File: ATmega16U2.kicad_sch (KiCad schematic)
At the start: 29 parts, among them J1 Conn_02x02_Odd_Even, J11 Conn_02x03_Odd_Even, J12 USB_B, U3 ATmega16U2-A, Y2 Crystal

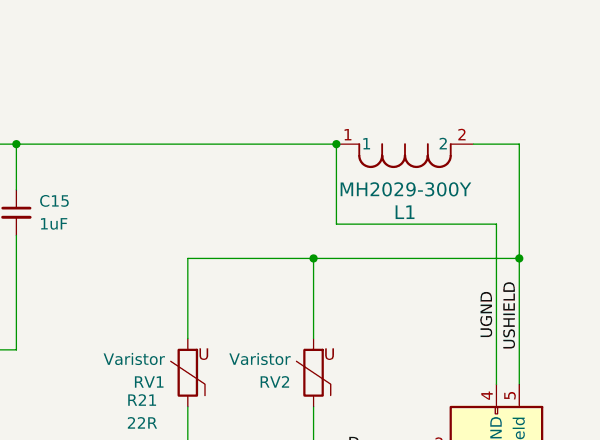
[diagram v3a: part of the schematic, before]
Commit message: finished editing the schematic and assigning footprints
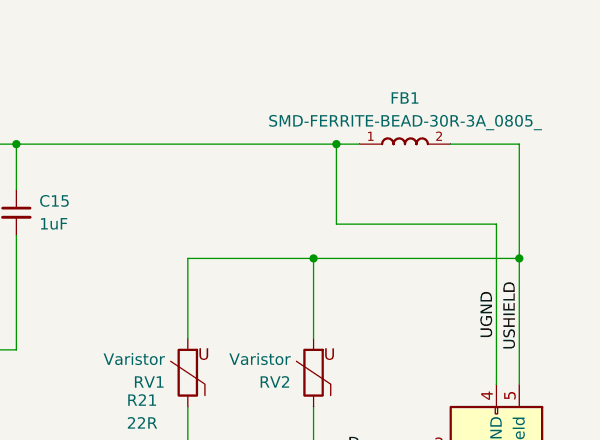
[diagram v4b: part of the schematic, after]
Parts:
- removed L1: MH2029-300Y, IND_BOURNS_MH2029, symbol MH2029_300Y:MH2029-300Y
- added FB1: SMD-FERRITE-BEAD-30R-3A_0805_, SMD-FERRITE-BEAD-30R-3A_0805_:L0805, symbol SMD-FERRITE-BEAD-30R-3A_0805_:SMD-FERRITE-BEAD-30R-3A_0805_
- J1: footprint (none) -> Connector_Hirose:Hirose_DF11-4DP-2DSA_2x02_P2.00mm_Vertical
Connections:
- net 1: now also FB1.1
- net USHIELD: now also FB1.2
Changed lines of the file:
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@@
 	)
 	(junction
+		(at 215.9 45.72)
+		(diameter 0)
+		(color 0 0 0 0)
+	)
+	(junction
 		(at 116.84 167.64)
 		(diameter 0)
@@
 	)
 	(junction
-		(at 215.9 45.72)
-		(diameter 0)
-		(color 0 0 0 0)
-	)
-	(junction
 		(at 58.42 74.93)
 		(diameter 0)
@@
 	(wire
 		(pts
+			(xy 228.6 45.72) (xy 236.22 45.72)
+		)
+		(stroke
+			(width 0)
+			(type default)
+		)
+	)
+	(wire
+		(pts
 			(xy 58.42 64.77) (xy 58.42 74.93)
 		)
@@
 	(wire
 		(pts
+			(xy 215.9 45.72) (xy 218.44 45.72)
+		)
+		(stroke
+			(width 0)
+			(type default)
+		)
+	)
+	(wire
+		(pts
 			(xy 124.46 152.4) (xy 124.46 148.59)
 		)
@@
 	(wire
 		(pts
-			(xy 236.22 45.72) (xy 231.14 45.72)
-		)
-		(stroke
-			(width 0)
-			(type default)
-		)
-	)
-	(wire
-		(pts
 			(xy 233.68 54.61) (xy 215.9 54.61)
 		)
@@
 			)
 		)
-		(property "Footprint" ""
+		(property "Footprint" "Connector_Hirose:Hirose_DF11-4DP-2DSA_2x02_P2.00mm_Vertical"
 			(at 78.74 100.33 0)
 			(effects
@@
 	)
 	(symbol
+		(lib_id "SMD-FERRITE-BEAD-30R-3A_0805_:SMD-FERRITE-BEAD-30R-3A_0805_")
+		(at 223.52 45.72 0)
+		(unit 1)
+		(exclude_from_sim no)
+		(in_bom yes)
+		(on_board yes)
+		(dnp no)
+		(fields_autoplaced yes)
+		(property "Reference" "FB1"
+			(at 223.52 40.64 0)
+			(effects
+				(font
+					(size 1.27 1.27)
+				)
+			)
+		)
+		(property "Value" "SMD-FERRITE-BEAD-30R-3A_0805_"
+			(at 223.52 43.18 0)
+			(effects
+				(font
+					(size 1.27 1.27)
+				)
+			)
+		)
+		(property "Footprint" "SMD-FERRITE-BEAD-30R-3A_0805_:L0805"
+			(at 223.52 45.72 0)
+			(effects
+				(font
+					(size 1.27 1.27)
+				)
+				(justify bottom)
+				(hide yes)
+			)
+		)
+		(property "Datasheet" ""
+			(at 223.52 45.72 0)
+			(effects
+				(font
+					(size 1.27 1.27)
+				)
+				(hide yes)
+			)
+		)
+		(property "Description" ""
+			(at 223.52 45.72 0)
+			(effects
+				(font
+					(size 1.27 1.27)
+				)
+				(hide yes)
+			)
+		)
+		(property "MF" "Bourns"
+			(at 223.52 45.72 0)
+			(effects
+				(font
+					(size 1.27 1.27)
+				)
+				(justify bottom)
+				(hide yes)
+			)
+		)
+		(property "Description_1" "\nCB2x1.2x.9mm, 30?25%3A, non-shdSMD | Bourns MH2029-300Y\n"
+			(at 223.52 45.72 0)
+			(effects
+				(font
+					(size 1.27 1.27)
+				)
+				(justify bottom)
+				(hide yes)
+			)
+		)
+		(property "Package" "0805 Bourns"
+			(at 223.52 45.72 0)
+			(effects
+				(font
+					(size 1.27 1.27)
+				)
+				(justify bottom)
+				(hide yes)
+			)
+		)
+		(property "MPN" "MH2029-300Y"
+			(at 223.52 45.72 0)
+			(effects
+				(font
+					(size 1.27 1.27)
+				)
+				(justify bottom)
+				(hide yes)
+			)
+		)
+		(property "Price" "None"
+			(at 223.52 45.72 0)
+			(effects
+				(font
+					(size 1.27 1.27)
+				)
+				(justify bottom)
+				(hide yes)
+			)
+		)
+		(property "VALUE" "30R 3A"
+			(at 223.52 45.72 0)
+			(effects
+				(font
+					(size 1.27 1.27)
+				)
+				(justify bottom)
+				(hide yes)
+			)
+		)
+		(property "SnapEDA_Link" "https://www.snapeda.com/parts/MH2029-300Y/Bourns+-+J.W.+Miller/view-part/?ref=snap"
+			(at 223.52 45.72 0)
+			(effects
+				(font
+					(size 1.27 1.27)
+				)
+				(justify bottom)
+				(hide yes)
+			)
+		)
+		(property "MP" "MH2029-300Y"
+			(at 223.52 45.72 0)
+			(effects
+				(font
+					(size 1.27 1.27)
+				)
+				(justify bottom)
+				(hide yes)
+			)
+		)
+		(property "Purchase-URL" "https://www.snapeda.com/api/url_track_click_mouser/?unipart_id=42623&manufacturer=Bourns&part_name=MH2029-300Y&search_term=mh2029"
+			(at 223.52 45.72 0)
+			(effects
+				(font
+					(size 1.27 1.27)
+				)
+				(justify bottom)
+				(hide yes)
+			)
+		)
+		(property "Availability" "In Stock"
+			(at 223.52 45.72 0)
+			(effects
+				(font
+					(size 1.27 1.27)
+				)
+				(justify bottom)
+				(hide yes)
+			)
+		)
+		(property "Check_prices" "https://www.snapeda.com/parts/MH2029-300Y/Bourns+-+J.W.+Miller/view-part/?ref=eda"
+			(at 223.52 45.72 0)
+			(effects
+				(font
+					(size 1.27 1.27)
+				)
+				(justify bottom)
+				(hide yes)
+			)
+		)
+		(pin "2"
+		)
+		(pin "1"
+		)
+		(instances
+			(project ""
+				(path "/01593c05-32ee-43cc-9d3f-a6fed62a39f4/b6f834a9-11ca-4a09-9cf4-5366685f0c51"
+					(reference "FB1")
+					(unit 1)
+				)
+			)
+		)
+	)
+	(symbol
 		(lib_id "Device:C_Small")
 		(at 200.66 92.71 0)
@@
 					(unit 1)
 				)
-			)
-		)
-	)
-	(symbol
-		(lib_id "MH2029_300Y:MH2029-300Y")
-		(at 231.14 45.72 180)
-		(unit 1)
-		(exclude_from_sim no)
-		(in_bom yes)
-		(on_board yes)
-		(dnp no)
-		(fields_autoplaced yes)
-		(property "Reference" "L1"
-			(at 223.52 53.34 0)
-			(effects
-				(font
-					(size 1.524 1.524)
-				)
-			)
-		)
-		(property "Value" "MH2029-300Y"
-			(at 223.52 50.8 0)
-			(effects
-				(font
-					(size 1.524 1.524)
-				)
-			)
-		)
-		(property "Footprint" "IND_BOURNS_MH2029"
-			(at 231.14 45.72 0)
-			(effects
-				(font
-					(size 1.27 1.27)
-					(italic yes)
-				)
-				(hide yes)
-			)
-		)
-		(property "Datasheet" "MH2029-300Y"
-			(at 231.14 45.72 0)
-			(effects
-				(font
-					(size 1.27 1.27)
-					(italic yes)
-				)
-				(hide yes)
-			)
-		)
-		(property "Description" ""
-			(at 231.14 45.72 0)
-			(effects
-				(font
-					(size 1.27 1.27)
-				)
-				(hide yes)
-			)
-		)
-		(pin "1"
-		)
-		(pin "2"
-		)
-		(instances
-			(project "arduino-mega-2560"
-				(path "/01593c05-32ee-43cc-9d3f-a6fed62a39f4/b6f834a9-11ca-4a09-9cf4-5366685f0c51"
-					(reference "L1")
-					(unit 1)
-				)

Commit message: started PCB design
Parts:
- Y2: footprint MCU-ATMEGA2560-16AU_TQFP100:TQFP100-0.5-14X14MM -> Crystal:Crystal_SMD_HC49-SD_HandSoldering
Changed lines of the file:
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@@
 			)
 		)
-		(property "Footprint" "MCU-ATMEGA2560-16AU_TQFP100:TQFP100-0.5-14X14MM"
+		(property "Footprint" "Crystal:Crystal_SMD_HC49-SD_HandSoldering"
 			(at 181.61 109.22 0)
 			(effects

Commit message: last save attempt
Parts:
- J1: footprint Connector_Hirose:Hirose_DF11-4DP-2DSA_2x02_P2.00mm_Vertical -> Connector_PinHeader_1.00mm:PinHeader_2x02_P1.00mm_Vertical
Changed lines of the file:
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@@
 			)
 		)
-		(property "Footprint" "Connector_Hirose:Hirose_DF11-4DP-2DSA_2x02_P2.00mm_Vertical"
+		(property "Footprint" "Connector_PinHeader_1.00mm:PinHeader_2x02_P1.00mm_Vertical"
 			(at 78.74 100.33 0)
 			(effects

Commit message: good progress
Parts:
- removed Y2: Crystal, Crystal:Crystal_SMD_HC49-SD_HandSoldering, symbol Device:Crystal
- added Y3: ECS-160-20-4X-B-DN, ECS_160_20_4X_B_DN:XTAL_ECS-160-20-4X-B-DN, symbol ECS-160-20-4X-B-DN:ECS-160-20-4X-B-DN
- RR1: renamed from 1M1; value R -> 1M
- RV1, RV2: footprint Varistor:Varistor_Panasonic_VF -> Resistor_SMD:R_0201_0603Metric_Pad0.64x0.40mm_HandSolder
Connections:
- net 1: now also Y3.1, Y3.2
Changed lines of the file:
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@@
 	)
 	(junction
-		(at 191.77 113.03)
+		(at 191.77 104.14)
 		(diameter 0)
 		(color 0 0 0 0)
@@
 	)
 	(junction
+		(at 180.34 104.14)
+		(diameter 0)
+		(color 0 0 0 0)
+	)
+	(junction
 		(at 166.37 45.72)
 		(diameter 0)
@@
 	)
 	(junction
-		(at 200.66 87.63)
+		(at 191.77 114.3)
 		(diameter 0)
 		(color 0 0 0 0)
 	)
 	(junction
-		(at 154.94 127)
+		(at 200.66 87.63)
 		(diameter 0)
 		(color 0 0 0 0)
 	)
 	(junction
-		(at 181.61 113.03)
+		(at 154.94 127)
 		(diameter 0)
 		(color 0 0 0 0)
@@
 	)
 	(junction
-		(at 181.61 105.41)
-		(diameter 0)
-		(color 0 0 0 0)
-	)
-	(junction
 		(at 236.22 58.42)
 		(diameter 0)
@@
 	)
 	(junction
-		(at 191.77 105.41)
+		(at 58.42 74.93)
 		(diameter 0)
 		(color 0 0 0 0)
 	)
 	(junction
-		(at 58.42 74.93)
+		(at 180.34 114.3)
 		(diameter 0)
 		(color 0 0 0 0)
@@
 		(at 137.16 86.36)
 	)
+	(bus_entry
+		(at 53.34 78.74)
+		(size 2.54 2.54)
+		(stroke
+			(width 0)
+			(type default)
+		)
+	)
 	(wire
 		(pts
@@
 	(wire
 		(pts
-			(xy 191.77 113.03) (xy 181.61 113.03)
+			(xy 110.49 137.16) (xy 110.49 146.05)
 		)
 		(stroke
@@
 	(wire
 		(pts
-			(xy 110.49 137.16) (xy 110.49 146.05)
+			(xy 154.94 53.34) (xy 154.94 39.37)
 		)
 		(stroke
@@
 	(wire
 		(pts
-			(xy 154.94 53.34) (xy 154.94 39.37)
+			(xy 58.42 74.93) (xy 53.34 74.93)
 		)
 		(stroke
@@
 	(wire
 		(pts
-			(xy 58.42 74.93) (xy 53.34 74.93)
+			(xy 199.39 82.55) (xy 198.12 82.55)
 		)
 		(stroke
@@
 	(wire
 		(pts
-			(xy 199.39 82.55) (xy 198.12 82.55)
+			(xy 172.72 104.14) (xy 172.72 106.68)
 		)
 		(stroke
@@
 	(wire
 		(pts
-			(xy 176.53 113.03) (xy 181.61 113.03)
+			(xy 176.53 114.3) (xy 180.34 114.3)
 		)
 		(stroke
@@
 	(wire
 		(pts
-			(xy 176.53 111.76) (xy 176.53 113.03)
+			(xy 191.77 104.14) (xy 191.77 105.41)
 		)
 		(stroke
@@
 	(wire
 		(pts
-			(xy 172.72 105.41) (xy 181.61 105.41)
+			(xy 172.72 104.14) (xy 180.34 104.14)
 		)
 		(stroke
@@
 	(wire
 		(pts
-			(xy 172.72 106.68) (xy 172.72 105.41)
+			(xy 102.87 109.22) (xy 137.16 109.22)
 		)
 		(stroke
@@
 	(wire
 		(pts
-			(xy 102.87 109.22) (xy 137.16 109.22)
+			(xy 176.53 111.76) (xy 176.53 114.3)
 		)
 		(stroke
@@
 	(wire
 		(pts
-			(xy 191.77 105.41) (xy 181.61 105.41)
+			(xy 172.72 111.76) (xy 176.53 111.76)
 		)
 		(stroke
@@
 	(wire
 		(pts
-			(xy 172.72 111.76) (xy 176.53 111.76)
+			(xy 124.46 167.64) (xy 124.46 163.83)
 		)
 		(stroke
@@
 	(wire
 		(pts
-			(xy 124.46 167.64) (xy 124.46 163.83)
+			(xy 180.34 104.14) (xy 191.77 104.14)
 		)
 		(stroke
@@
 	(wire
 		(pts
+			(xy 191.77 114.3) (xy 191.77 113.03)
+		)
+		(stroke
+			(width 0)
+			(type default)
+		)
+	)
+	(wire
+		(pts
 			(xy 213.36 58.42) (xy 236.22 58.42)
 		)
@@
 	(wire
 		(pts
-			(xy 191.77 102.87) (xy 191.77 105.41)
+			(xy 191.77 102.87) (xy 191.77 104.14)
+		)
+		(stroke
+			(width 0)
+			(type default)
+		)
+	)
+	(wire
+		(pts
+			(xy 180.34 114.3) (xy 191.77 114.3)
 		)
 		(stroke
@@
 	(wire
 		(pts
-			(xy 191.77 115.57) (xy 191.77 113.03)
+			(xy 191.77 115.57) (xy 191.77 114.3)
 		)
 		(stroke
@@
 	)
 	(label "1"
-		(at 181.61 105.41 270)
+		(at 181.61 104.14 270)
 		(fields_autoplaced yes)
 		(effects
@@
 	)
 	(label "2"
-		(at 181.61 113.03 90)
+		(at 181.61 114.3 90)
 		(fields_autoplaced yes)
 		(effects
@@
 	)
 	(label "XT1"
-		(at 184.15 113.03 0)
+		(at 184.15 114.3 0)
 		(fields_autoplaced yes)
 		(effects
@@
 	)
 	(label "XT2"
-		(at 184.15 105.41 0)
+		(at 184.15 104.14 0)
 		(fields_autoplaced yes)
 		(effects
@@
 			)
 		)
-		(property "Footprint" "Varistor:Varistor_Panasonic_VF"
+		(property "Footprint" "Resistor_SMD:R_0201_0603Metric_Pad0.64x0.40mm_HandSolder"
 			(at 215.138 71.12 90)
 			(effects
@@
 		(dnp no)
 		(fields_autoplaced yes)
-		(property "Reference" "1M1"
+		(property "Reference" "RR1"
 			(at 194.31 107.9499 0)
 			(effects
@@
 			)
 		)
-		(property "Value" "R"
+		(property "Value" "1M"
 			(at 194.31 110.4899 0)
 			(effects
@@
 			(project "arduino-mega-2560"
 				(path "/01593c05-32ee-43cc-9d3f-a6fed62a39f4/b6f834a9-11ca-4a09-9cf4-5366685f0c51"
-					(reference "1M1")
+					(reference "RR1")
 					(unit 1)
 				)
@@
 			)
 		)
-		(property "Footprint" "Varistor:Varistor_Panasonic_VF"
+		(property "Footprint" "Resistor_SMD:R_0201_0603Metric_Pad0.64x0.40mm_HandSolder"
 			(at 201.168 71.12 90)
 			(effects
@@
 	)
 	(symbol
-		(lib_id "Device:Crystal")
-		(at 181.61 109.22 270)
-		(unit 1)
-		(exclude_from_sim no)
-		(in_bom yes)
-		(on_board yes)
-		(dnp no)
-		(fields_autoplaced yes)
-		(property "Reference" "Y2"
-			(at 177.8 110.4901 90)
-			(effects
-				(font
-					(size 1.27 1.27)
-				)
-				(justify right)
-			)
-		)
-		(property "Value" "Crystal"
-			(at 177.8 107.9501 90)
-			(effects
-				(font
-					(size 1.27 1.27)
-				)
-				(justify right)
-			)
-		)
-		(property "Footprint" "Crystal:Crystal_SMD_HC49-SD_HandSoldering"
-			(at 181.61 109.22 0)
-			(effects
-				(font
-					(size 1.27 1.27)
-				)
-				(hide yes)
-			)
-		)
-		(property "Datasheet" "~"
-			(at 181.61 109.22 0)
-			(effects
-				(font
-					(size 1.27 1.27)
-				)
-				(hide yes)
-			)
-		)
-		(property "Description" "Two pin crystal"
-			(at 181.61 109.22 0)
-			(effects
-				(font
-					(size 1.27 1.27)
-				)
-				(hide yes)
-			)
-		)
-		(pin "2"
-		)
-		(pin "1"
-		)
-		(instances
-			(project "arduino-mega-2560"
-				(path "/01593c05-32ee-43cc-9d3f-a6fed62a39f4/b6f834a9-11ca-4a09-9cf4-5366685f0c51"
-					(reference "Y2")
-					(unit 1)
-				)
-			)
-		)
-	)
-	(symbol
 		(lib_id "power:+5V")
 		(at 124.46 148.59 270)
@@
 					(unit 1)
 				)
+			)
+		)
+	)
+	(symbol
+		(lib_id "ECS-160-20-4X-B-DN:ECS-160-20-4X-B-DN")
+		(at 180.34 109.22 90)
+		(mirror x)
+		(unit 1)
+		(exclude_from_sim no)
+		(in_bom yes)
+		(on_board yes)
+		(dnp no)
+		(property "Reference" "Y3"
+			(at 182.372 109.22 90)
+			(effects
+				(font
+					(size 1.27 1.27)
+				)
+				(justify right)
+			)
+		)
+		(property "Value" "ECS-160-20-4X-B-DN"
+			(at 177.292 120.65 0)
+			(effects
+				(font
+					(size 1.27 1.27)
+				)
+				(justify right)
+			)
+		)
+		(property "Footprint" "ECS_160_20_4X_B_DN:XTAL_ECS-160-20-4X-B-DN"
+			(at 180.34 109.22 0)
+			(effects
+				(font
+					(size 1.27 1.27)
+				)
+				(justify bottom)
+				(hide yes)
+			)
+		)
+		(property "Datasheet" ""
+			(at 180.34 109.22 0)
+			(effects
+				(font
+					(size 1.27 1.27)
+				)
+				(hide yes)
+			)
+		)
+		(property "Description" ""
+			(at 180.34 109.22 0)
+			(effects
+				(font
+					(size 1.27 1.27)
+				)
+				(hide yes)
+			)
+		)
+		(pin "1"
+		)
+		(pin "2"
+		)
+		(instances
+			(project ""
+				(path "/01593c05-32ee-43cc-9d3f-a6fed62a39f4/b6f834a9-11ca-4a09-9cf4-5366685f0c51"
+					(reference "Y3")
+					(unit 1)
+				)

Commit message: final edit
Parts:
- removed R19: 1K, Resistor_SMD:R_0201_0603Metric_Pad0.64x0.40mm_HandSolder, symbol Device:R
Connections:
- net +5V: no longer C14.2, C16.2, C17.1, C18.1, J11.6 (Pin_6), JP1.2 (B)
- net 4: no longer C13.1, U3.13 (~{HWB}/PD7)
- new net DTR: C13.1, U3.13 (~{HWB}/PD7)
- new net GND: C14.2, C16.2, C17.1, C18.1, J11.6 (Pin_6), JP1.2 (B)
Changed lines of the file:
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@@
-	)
-	(junction
-		(at 130.81 60.96)
-		(diameter 0)
-		(color 0 0 0 0)
 	)
 	(junction
@@
 	(wire
 		(pts
-			(xy 130.81 60.96) (xy 130.81 57.15)
-		)
-		(stroke
-			(width 0)
-			(type default)
-		)
-	)
-	(wire
-		(pts
 			(xy 180.34 50.8) (xy 180.34 45.72)
 		)
@@
 	(wire
 		(pts
-			(xy 137.16 60.96) (xy 130.81 60.96)
+			(xy 121.92 60.96) (xy 137.16 60.96)
 		)
 		(stroke
@@
 		(pts
 			(xy 226.06 87.63) (xy 218.44 87.63)
-		)
-		(stroke
-			(width 0)
-			(type default)
-		)
-	)
-	(wire
-		(pts
-			(xy 130.81 60.96) (xy 121.92 60.96)
 		)
 		(stroke
@@
 		)
 	)
-	(label "5"
-		(at 130.81 49.53 90)
-		(fields_autoplaced yes)
-		(effects
-			(font
-				(size 1.27 1.27)
-			)
-			(justify left bottom)
-		)
-	)
 	(label "SCK2"
 		(at 125.73 114.3 0)
@@
 	(label "5"
 		(at 66.04 80.01 180)
-		(fields_autoplaced yes)
-		(effects
-			(font
-				(size 1.27 1.27)
-			)
-			(justify right bottom)
-		)
-	)
-	(label "4"
-		(at 130.81 57.15 270)
 		(fields_autoplaced yes)
 		(effects
@@
 	)
 	(symbol
-		(lib_id "power:GND")
-		(at 130.81 49.53 180)
-		(unit 1)
-		(exclude_from_sim no)
-		(in_bom yes)
-		(on_board yes)
-		(dnp no)
-		(fields_autoplaced yes)
-		(property "Reference" "#PWR032"
-			(at 130.81 43.18 0)
-			(effects
-				(font
-					(size 1.27 1.27)
-				)
-				(hide yes)
-			)
-		)
-		(property "Value" "GND"
-			(at 130.81 44.45 0)
-			(effects
-				(font
-					(size 1.27 1.27)
-				)
-			)
-		)
-		(property "Footprint" ""
-			(at 130.81 49.53 0)
-			(effects
-				(font
-					(size 1.27 1.27)
-				)
-				(hide yes)
-			)
-		)
-		(property "Datasheet" ""
-			(at 130.81 49.53 0)
-			(effects
-				(font
-					(size 1.27 1.27)
-				)
-				(hide yes)
-			)
-		)
-		(property "Description" "Power symbol creates a global label with name \"GND\" , ground"
-			(at 130.81 49.53 0)
-			(effects
-				(font
-					(size 1.27 1.27)
-				)
-				(hide yes)
-			)
-		)
-		(pin "1"
-		)
-		(instances
-			(project "arduino-mega-2560"
-				(path "/01593c05-32ee-43cc-9d3f-a6fed62a39f4/b6f834a9-11ca-4a09-9cf4-5366685f0c51"
-					(reference "#PWR032")
-					(unit 1)
-				)
-			)
-		)
-	)
-	(symbol
 		(lib_id "Device:R")
 		(at 124.46 160.02 180)
@@
 					(unit 1)
 				)
-			)
-		)
-	)
-	(symbol
-		(lib_id "Device:R")
-		(at 130.81 53.34 0)
-		(mirror y)
-		(unit 1)
-		(exclude_from_sim no)
-		(in_bom yes)
-		(on_board yes)
-		(dnp no)
-		(property "Reference" "R19"
-			(at 124.46 53.34 90)
-			(effects
-				(font
-					(size 1.27 1.27)
-				)
-			)
-		)
-		(property "Value" "1K"
-			(at 127 53.34 90)
-			(effects
-				(font
-					(size 1.27 1.27)
-				)
-			)
-		)
-		(property "Footprint" "Resistor_SMD:R_0201_0603Metric_Pad0.64x0.40mm_HandSolder"
-			(at 132.588 53.34 90)
-			(effects
-				(font
-					(size 1.27 1.27)
-				)
-				(hide yes)
-			)
-		)
-		(property "Datasheet" "~"
-			(at 130.81 53.34 0)
-			(effects
-				(font
-					(size 1.27 1.27)
-				)
-				(hide yes)
-			)
-		)
-		(property "Description" "Resistor"
-			(at 130.81 53.34 0)
-			(effects
-				(font
-					(size 1.27 1.27)
-				)
-				(hide yes)
-			)
-		)
-		(pin "2"
-		)
-		(pin "1"
-		)
-		(instances
-			(project "arduino-mega-2560"
-				(path "/01593c05-32ee-43cc-9d3f-a6fed62a39f4/b6f834a9-11ca-4a09-9cf4-5366685f0c51"
-					(reference "R19")
-					(unit 1)
-				)
